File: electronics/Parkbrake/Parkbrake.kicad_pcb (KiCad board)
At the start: 2 copper layers, 101.6 x 114.3 mm, 353 parts, among them P1 Conn48pin, P2 JTAG, P3 UART, Q1 BSS138, Q10 IPD031N06L3 G, Q11 IPD031N06L3 G, Q12 NX3008CBKS, Q13 NX3008CBKS, Q14 IPD031N06L3 G, Q15 IPD031N06L3 G, Q16 IPD031N06L3 G, Q17 IPD031N06L3 G, Q18 NX3008CBKS, Q19 NX3008CBKS, Q2 BSS138, Q20 IPD031N06L3 G, Q21 IPD031N06L3 G, Q22 IPD031N06L3 G, Q23 IPD031N06L3 G, Q24 NX3008CBKS, Q25 NX3008CBKS, Q26 IPD031N06L3 G, Q27 IPD031N06L3 G, Q28 IPD031N06L3 G, Q29 IPD031N06L3 G, Q3 P-ch -40V 0.0035ohm, Q30 NX3008CBKS, Q31 BSS138, Q32 NTS4173, Q33 NX3008CBKS, Q4 P-ch -40V 0.0035ohm, Q5 BSS308, Q6 BSS308, Q7 NX3008CBKS, Q8 IPD031N06L3 G, Q9 IPD031N06L3 G, U1 74LVC00, U10 IRS2304, U11 ZXCT1082, U12 IRS2304, U13 LM2903, U14 IRS2304, U15 ZXCT1082, U16 IRS2304, U17 LM2903, U18 IRS2304, U19 ZXCT1082, U2 74LVC08, U20 IRS2304, U21 MIC2619, U22 MC34063, U23 LD1117S33CTR, U24 CAT25160_EEPROM, U25 STM32F373RBTx, U26 SN65HVD1050D, U27 SN74LVC245ADBR, U28 SN74HC20, U29 SN74HC02, U3 74LVC00, U30 SN74HC132, U31 MAX232, U32 MAX232, U33 NCV1124, U34 NCV1124, U35 74LVC08, U4 74LVC08, U5 LM2903, U6 IRS2304, U7 ZXCT1082, U8 IRS2304, U9 LM2903, Y1 24Mhz

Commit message: traceroute finished although there probably is some errors
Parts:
- C22, C29, C33, C48, C49, C50, C51, C52, C53, C54, C55, C56, C58, C60, C61, C9, D28, R92, R93, R98, R99: moved to B.Cu
- JP1: value Jumper_NO_Small -> BOOT0
- moved C58 263.1 mm to (114.1, 103.5), turned to 180 degrees
- moved C49 255.6 mm to (108.7, 145.0), turned to 180 degrees
- moved C45 252.4 mm to (111.6, 122.0), turned to 180 degrees
- moved C50 252.1 mm to (108.2, 147.6), turned to 180 degrees
- moved R96 251.1 mm to (139.9, 149.7), turned to 180 degrees
- moved C53 250.4 mm to (104.7, 143.0), turned to 270 degrees
- moved R91 246.5 mm to (148.6, 149.7), turned to 180 degrees
- moved R90 246.0 mm to (152.8, 149.6), turned to 180 degrees
- moved R94 245.1 mm to (157.3, 145.4), turned to 90 degrees
- moved C54 245.0 mm to (101.8, 143.5), turned to 270 degrees
- moved R97 244.6 mm to (135.9, 149.7), turned to 180 degrees
- moved C52 243.4 mm to (109.0, 133.7), turned to 270 degrees
- moved C60 241.7 mm to (142.3, 149.7)
- moved R92 240.6 mm to (160.6, 135.0), turned to 180 degrees
- moved C44 240.4 mm to (115.5, 122.0)
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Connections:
- C41 pad 1: Net-(C41-Pad1) -> +3.3V
- R92 pad 2: USART_TX -> USART_RX
- R93 pad 1: USART_RX -> USART_TX
- U27 pad 11: SAFE_TO_RELEASE -> IGN_ON_SIGNAL
- U27 pad 13: IGN_ON_SIGNAL -> SAFE_TO_RELEASE
- U27 pad 7: IGN_ON_SIG -> RELEASE_CMD_SIG
- U27 pad 9: RELEASE_CMD_SIG -> IGN_ON_SIG
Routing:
- net LR_wheelsensor_in-: track 577.0 -> 924.8 mm, vias 23 -> 34
- net +3.3V: track 278.8 -> 621.5 mm, vias 14 -> 27
- net INDICATOR_ON: track 0.00 -> 110.6 mm, vias 0 -> 5
- net Bridge_Disable: track 32.7 -> 132.5 mm, vias 2 -> 6
- net +5V: track 151.1 -> 242.8 mm, vias 7 -> 11
- net gate_drive_24V: track 136.2 -> 217.9 mm, vias 8 -> 14
- net LIGHTS_ON_SIG: track 0.00 -> 80.8 mm, vias 0 -> 3
- net VR_diag_test: track 0.00 -> 75.8 mm, vias 0 -> 2
- net IGN_ON_SIG: track 0.00 -> 73.5 mm, vias 0 -> 3
- net Feed_voltsense: track 0.00 -> 72.3 mm, vias 0 -> 1
- net LeftRear_DIAG: track 12.7 -> 78.0 mm
- net RightRear_DIAG: track 17.5 -> 80.4 mm
- net Enable_Bridge_PWR: track 89.6 -> 151.1 mm, vias 2 -> 6
- net TIGHTEN_CMD_SIG: track 0.00 -> 60.9 mm, vias 0 -> 1
- net RightRear_Tighten: track 23.3 -> 83.6 mm
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
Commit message: DRC pass!
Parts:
- moved C43 15.4 mm to (136.1, 143.2), turned to 0 degrees
- moved C42 14.0 mm to (140.4, 143.2), turned to 180 degrees
- moved U24 10.0 mm to (138.3, 140.1), turned to 0 degrees
- moved R94 4.95 mm to (152.9, 143.2), turned to 180 degrees
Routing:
- net GNDPWR: track 594.6 -> 725.4 mm
- net LeftRearMotor-: track 64.5 -> 122.2 mm, vias 6 -> 11
- net +12V_powerFront: track 262.3 -> 318.6 mm
- net +3.3V: track 621.5 -> 566.1 mm
- net +5V: track 242.8 -> 289.8 mm, vias 11 -> 13
- net LR_wheelsensor_in-: track 924.8 -> 967.1 mm, vias 34 -> 37
- net Net-(U31-Pad12): track 37.2 -> 0.00 mm, vias 1 -> 0
- net Net-(Q26-Pad2): track 36.0 -> 62.3 mm
- net +12V_powerRear: track 224.7 -> 241.9 mm, vias 11 -> 14
- net /microcontroller/SPI_MISO: track 47.9 -> 34.2 mm
- net Net-(U3-Pad11): track 9.98 -> 23.0 mm, vias 0 -> 2
- net Net-(Q11-Pad3): track 34.2 -> 46.3 mm
- net /microcontroller/SPI_CS: track 44.0 -> 33.0 mm
- net Net-(Q27-Pad3): track 21.3 -> 31.1 mm
- net LIGHTS_ON_SIG: track 80.8 -> 73.9 mm
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
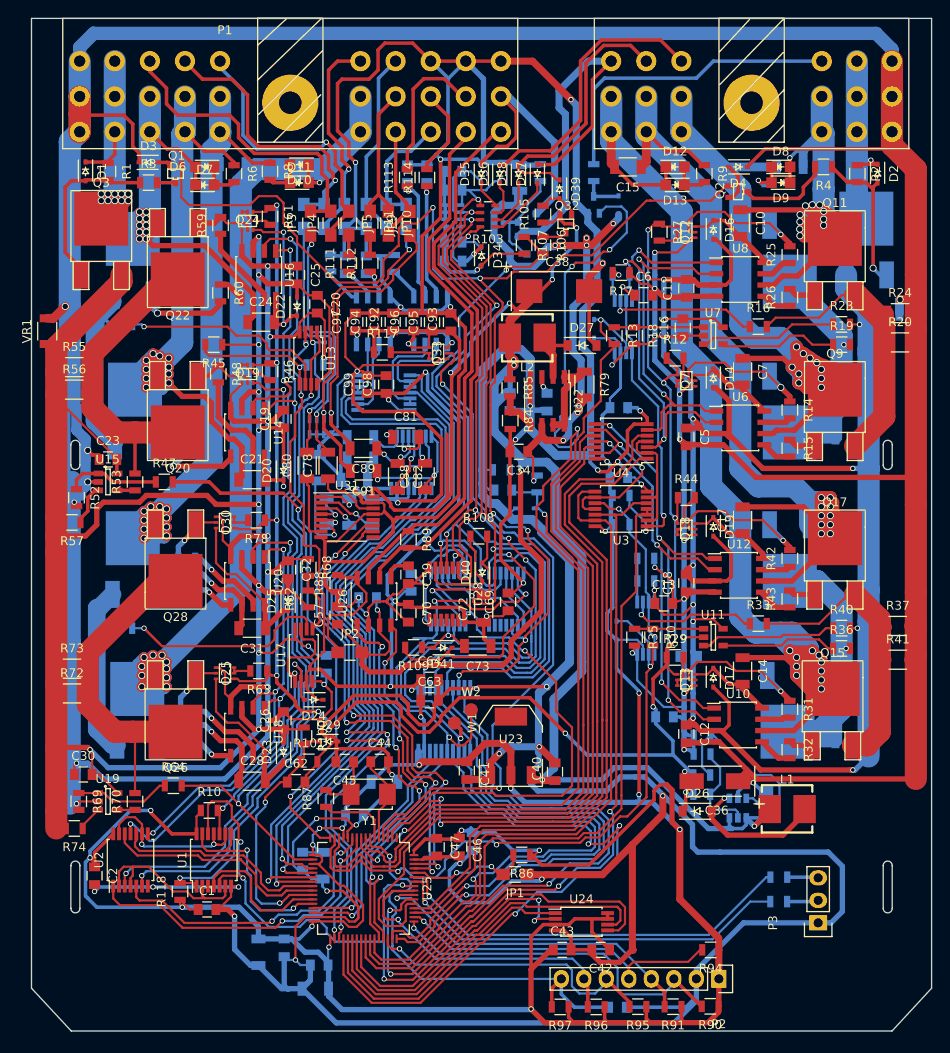
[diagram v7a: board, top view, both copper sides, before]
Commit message: Component ids moved and removed silkscreen for high current copper, solder strengthed copper
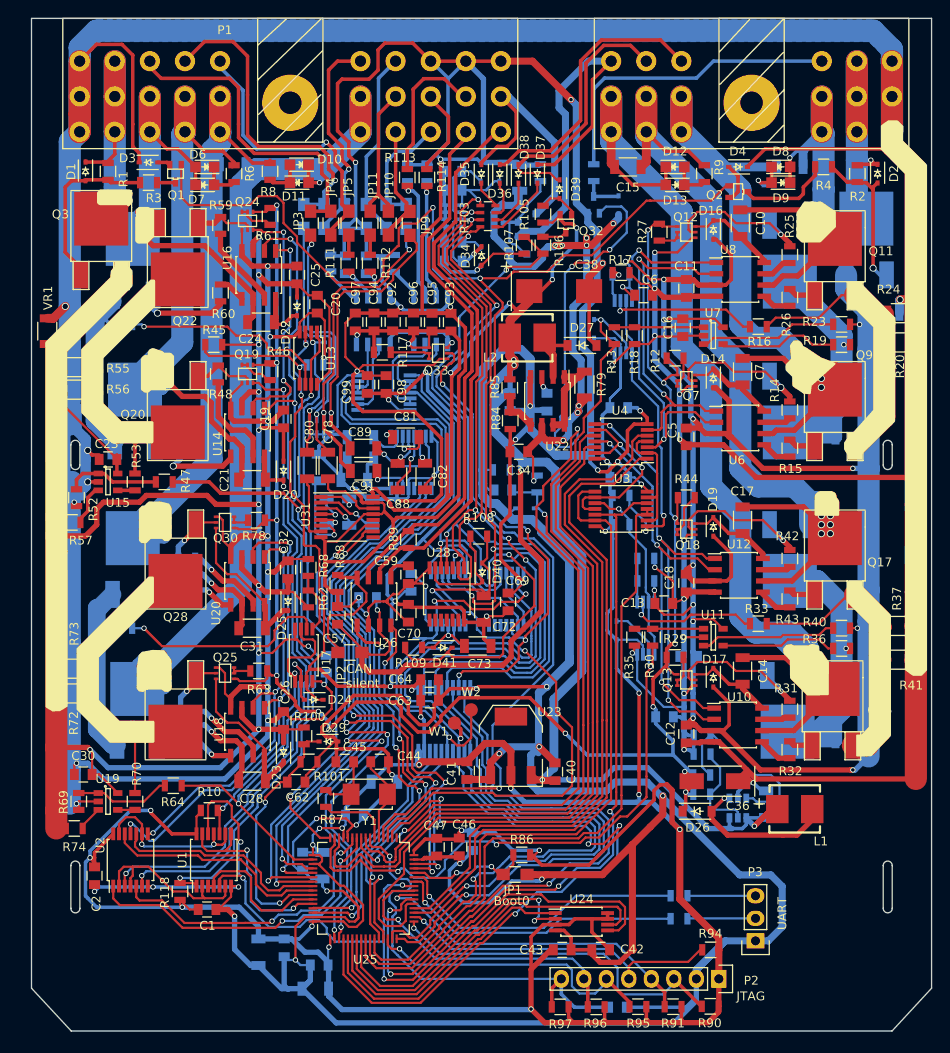
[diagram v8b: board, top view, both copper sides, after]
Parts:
- moved R92 11.5 mm to (149.3, 137.1)
- moved R93 11.4 mm to (149.3, 139.7)
- moved P3 7.36 mm to (157.9, 142.2)
- moved L1 0.86 mm to (162.4, 127.4)
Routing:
- net GNDPWR: track 725.4 -> 748.7 mm
- net USART_RX: track 46.6 -> 33.8 mm
- net USART_TX: track 45.8 -> 33.8 mm
- net /+12V_BatR: track 23.3 -> 31.2 mm
- net /+12V_BatF: track 61.2 -> 69.2 mm
- net L_wheelsensor_out-: track 32.0 -> 36.4 mm
- net Net-(P3-Pad2): track 3.57 -> 7.81 mm
- net Net-(P3-Pad3): track 3.63 -> 7.69 mm
- net RightFrontMotor-: track 142.8 -> 146.8 mm
- net LeftRearMotor-: track 122.2 -> 126.2 mm
- net LeftFrontMotor-: track 89.7 -> 93.7 mm
- net RightRearMotor-: track 166.7 -> 170.7 mm
- net RightRearMotor+: track 198.7 -> 202.7 mm
- net RightFrontMotor+: track 161.7 -> 165.6 mm
- net LeftRearMotor+: track 160.5 -> 164.5 mm
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- added copper zone on B.Cu, net GNDPWR
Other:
- board text added: "Boot0"
- board text added: "CAN silent"
